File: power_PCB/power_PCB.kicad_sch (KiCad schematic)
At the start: 0 parts

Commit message: all boards routed: light rev B (SOT-23 switches, protected input), pump rev B (CSD18540 MOSFETs), power rev A1 (parts selected), brain Micro-Fit connectors + display on edge; whitelist gitignore
Light, power and pump pass DRC and ERC clean. Brain routed with 0 unconnected; remaining warnings are dangling vias, thin silk text and missing no-connect flags. All cable connectors standardized to Molex Micro-Fit 3.0. Repo now tracks only the KiCad project files, design rules, local libraries and brain 3D models.
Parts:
- added C1, C17: 100uF 35V HYBRID, Capacitor_SMD:CP_Elec_8x10.5, symbol Device:C_Polarized
- added C10, C11, C15, C2, C4, C5: 100nF 50V X7R, Capacitor_SMD:C_0805_2012Metric, symbol Device:C
- added C12, C13, C6, C7: 22uF 25V X7R, Capacitor_SMD:C_1210_3225Metric, symbol Device:C
- added C14, C8: 75pF 50V C0G 5%, Capacitor_SMD:C_0805_2012Metric, symbol Device:C
- added C16: 1uF 25V X7R, Capacitor_SMD:C_0805_2012Metric, symbol Device:C
- added C3, C9: 10uF 50V X7R, Capacitor_SMD:C_1210_3225Metric, symbol Device:C
- added D1: SMBJ15A, Diode_SMD:D_SMB, symbol Device:D_TVS
- added D2: V10P45 / 10A 45V, HydroPower:Vishay_V10P45_TO-277A_K1_A2, symbol Device:D_Schottky
- added F1: 20A FAST / PROVISIONAL, Fuse:Fuse_Littelfuse-NANO2-451_453, symbol Device:Fuse
- added F2: 5A FAST / PROVISIONAL, Fuse:Fuse_Littelfuse-NANO2-451_453, symbol Device:Fuse
- added F3, F5: 3A FAST / PROVISIONAL, Fuse:Fuse_Littelfuse-NANO2-451_453, symbol Device:Fuse
- added F4: 15A FAST / PROVISIONAL, Fuse:Fuse_Littelfuse-NANO2-451_453, symbol Device:Fuse
- added J1: 12V INPUT - 5 PAIRS, Connector_Molex:Molex_Micro-Fit_3.0_43650-1024_1x10-1MP_P3.00mm_Vertical, symbol Connector_Generic:Conn_01x10
- added J2: LIGHT BOARD, Connector_Molex:Molex_Micro-Fit_3.0_43650-0224_1x02-1MP_P3.00mm_Vertical, symbol Connector_Generic:Conn_01x02
- added J3: PUMP BOARD, Connector_Molex:Molex_Micro-Fit_3.0_43650-0324_1x03-1MP_P3.00mm_Vertical, symbol Connector_Generic:Conn_01x03
- added J4: COOLER - 3 PAIRS, Connector_Molex:Molex_Micro-Fit_3.0_43650-0624_1x06-1MP_P3.00mm_Vertical, symbol Connector_Generic:Conn_01x06
- added J5: BRAIN POWER, Connector_Molex:Molex_Micro-Fit_3.0_43650-0224_1x02-1MP_P3.00mm_Vertical, symbol Connector_Generic:Conn_01x02
- added J6: COOLER CONTROL, Connector_Molex:Molex_Micro-Fit_3.0_43650-0224_1x02-1MP_P3.00mm_Vertical, symbol Connector_Generic:Conn_01x02
- added L1: 6.8uH, Inductor_SMD:L_Coilcraft_XAL7030-682, symbol Device:L
- added L2: 10uH, Inductor_SMD:L_Coilcraft_XAL7030-103, symbol Device:L
- added Q1: CSD18540Q5B, Package_TO_SOT_SMD:TDSON-8-1, symbol Transistor_FET:CSD18540Q5B
- added R1, R5: 511k 1%, Resistor_SMD:R_0603_1608Metric, symbol Device:R
- added R10, R11: 22R, Resistor_SMD:R_0603_1608Metric, symbol Device:R
- added R12, R9: 10k, Resistor_SMD:R_0603_1608Metric, symbol Device:R
- added R2, R6: 105k 1%, Resistor_SMD:R_0603_1608Metric, symbol Device:R
- added R3, R7: 100k 0.1%, Resistor_SMD:R_0603_1608Metric, symbol Device:R
- added R4: 22.1k 0.1%, Resistor_SMD:R_0603_1608Metric, symbol Device:R
- added R8: 13.5k 0.1%, Resistor_SMD:R_0603_1608Metric, symbol Device:R
- added TP1: GND, HydroPower:TestPoint_Pad_D2.0mm_ClearSilk, symbol Connector:TestPoint
- added TP2: P12V, HydroPower:TestPoint_Pad_D2.0mm_ClearSilk, symbol Connector:TestPoint
- added TP3: +3V3, HydroPower:TestPoint_Pad_D2.0mm_ClearSilk, symbol Connector:TestPoint
- added TP4: +5V, HydroPower:TestPoint_Pad_D2.0mm_ClearSilk, symbol Connector:TestPoint
- added TP5: COOL_NEG, HydroPower:TestPoint_Pad_D2.0mm_ClearSilk, symbol Connector:TestPoint
- added U1, U2: TPS54302DDCR, Package_TO_SOT_SMD:SOT-23-6, symbol Regulator_Switching:TPS54302
- added U3: UCC27511ADBVR, Package_TO_SOT_SMD:SOT-23-6, symbol Driver_FET:UCC27511ADBV
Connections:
- new net: C14.2, R7.2, R8.1, U2.4 (FB)
- new net: C11.2, L2.1, U2.2 (SW)
- new net: R5.2, R6.1, U2.5 (EN)
- new net: C11.1, U2.6 (BOOT)
- new net: Q1.4 (G), R10.2, R11.2, R12.1
- new net: C5.1, U1.6 (BOOT)
- new net: C5.2, L1.1, U1.2 (SW)
- new net: R1.2, R2.1, U1.5 (EN)
- new net: R10.1, U3.2 (OUTH)
- new net: R11.1, U3.3 (OUTL)
- new net: C8.2, R3.2, R4.1, U1.4 (FB)
- new net +3V3: C6.1, C7.1, C8.1, J5.1 (Pin_1), L1.2, R3.1, TP3.1
- new net +5V: C12.1, C13.1, C14.1, C15.1, C16.1, J3.2 (Pin_2), L2.2, R7.1, TP4.1, U3.1 (V_{DD})
- new net COOL_12V: C17.1, D2.1 (K), F4.2, J4.1 (Pin_1), J4.2 (Pin_2), J4.3 (Pin_3)
- new net COOL_EN: J6.1 (Pin_1), R9.1, U3.6 (IN+)
- new net COOL_NEG: D2.2 (A), J4.4 (Pin_4), J4.5 (Pin_5), J4.6 (Pin_6), Q1.5 (D), TP5.1
- new net GND: C1.2, C10.2, C12.2, C13.2, C15.2, C16.2, C17.2, C2.2, C3.2, C4.2, C6.2, C7.2, C9.2, D1.2 (A2), J1.10 (Pin_10), J1.6 (Pin_6), J1.7 (Pin_7), J1.8 (Pin_8), J1.9 (Pin_9), J2.2 (Pin_2), J3.3 (Pin_3), J5.2 (Pin_2), J6.2 (Pin_2), Q1.1 (S), Q1.2 (S), Q1.3 (S), R12.2, R2.2, R4.2, R6.2, R8.2, R9.2, TP1.1, U1.1 (GND), U2.1 (GND), U3.4 (GND), U3.5 (IN-)
- new net LIGHT_12V: F2.2, J2.1 (Pin_1)
- new net LOGIC_12V: C10.1, C3.1, C4.1, C9.1, F5.2, R1.1, R5.1, U1.3 (VIN), U2.3 (VIN)
- new net P12V: C1.1, C2.1, D1.1 (A1), F1.2, F2.1, F3.1, F4.1, F5.1, TP2.1
- new net PUMP_12V: F3.2, J3.1 (Pin_1)
- new net VIN_12V: F1.1, J1.1 (Pin_1), J1.2 (Pin_2), J1.3 (Pin_3), J1.4 (Pin_4), J1.5 (Pin_5)
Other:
- note added: "1. 12V INPUT / FUSED DISTRIBUTION"
- note added: "2. 12V TO +3V3 BUCK - TPS54302"
- note added: "3. 12V TO +5V BUCK - TPS54302"
- note added: "4. COOLER SWITCH - PE8 HIGH = ON"
- note added: "5. TEST POINTS / RELEASE NOTES"
- note added: "Cooler estimate: 120W / 12V = 10A ONLY if 120W is electrical input. Confirm total current including its fan and any water circulation pump. Low-side switch: COOL_NEG must not have another ground connection. Use slow on/off control; no high-frequency PWM specified. Driver IN- grounded; IN+ and gate pulled down for disconnected control. Q1 requires heat-spreading copper; final thermal validation pe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"
- note added: "J1: pins 1-5 = +12V input; pins 6-10 = GND. Use all five 18AWG wires per polarity. J4: pins 1-3 = fused +12V; pins 4-6 = COOL_NEG. Use all three 18AWG wires per polarity. Equal wire lengths and sound crimps required; validate contact current sharing / temperature. Provisional total continuous budget: 15A at room temperature; further derating in warm enclosure. Fuses are provisional: F1 20A, F2 5A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"
- note added: "J6 pin 1 -> brain J9 pin 3 (PE8 / COOL) J6 pin 2 -> brain J9 pin 1 (GND) J5 pin 1 -> brain J10 pin 1 (3V3); pin 2 -> GND."
- note added: "PRE-LAYOUT PART SELECTION - NOT FOR FABRICATION MPN, Manufacturer and Datasheet fields assigned to every purchased PCB part. All soldered parts / connector tabs are surface mount; test points are bare copper. Current-dependent selections remain provisional until loads / temperature are measured. Brain supply is 3.3V ONLY. Verify it before connecting the brain. 5V pump rail retained pending teamma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"
- note added: "Short VIN bypass / SW loop; sense FB at output capacitors. Coilcraft XAL7030 selected. Initial rail load target 1A; validate DC bias, loop response and temperature. IC 3A is not a board rating."
- title: (none) -> HYDROPONICS - POWER DISTRIBUTION AND COOLER CONTROL

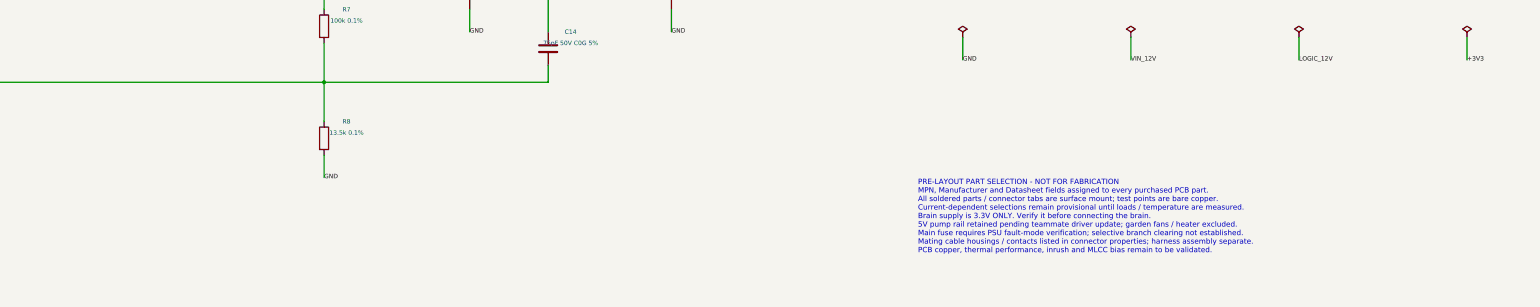
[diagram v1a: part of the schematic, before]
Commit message: Update four KiCad designs and include portable project libraries
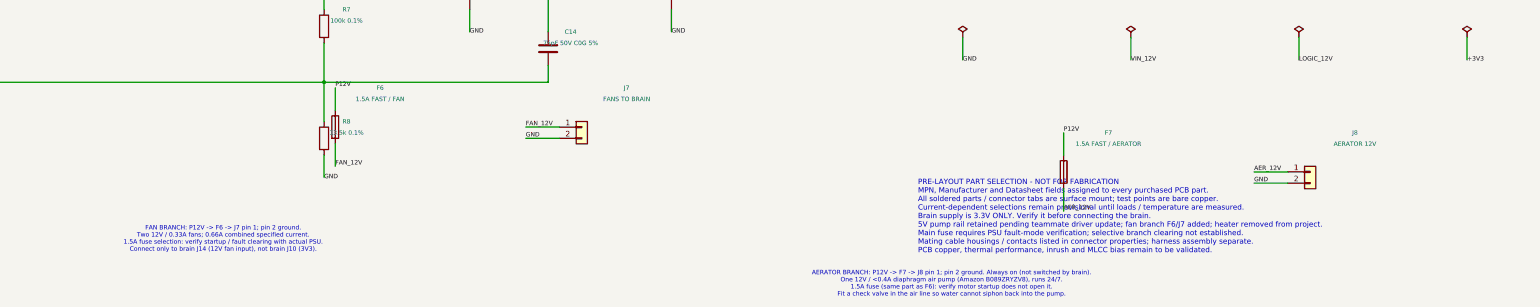
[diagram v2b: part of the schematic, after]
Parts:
- added F6: 1.5A FAST / FAN, Fuse:Fuse_1206_3216Metric, symbol Device:Fuse
- added F7: 1.5A FAST / AERATOR, Fuse:Fuse_1206_3216Metric, symbol Device:Fuse
- added J7: FANS TO BRAIN, Connector_JST:JST_XH_B2B-XH-A_1x02_P2.50mm_Vertical, symbol Connector_Generic:Conn_01x02
- added J8: AERATOR 12V, Connector_JST:JST_XH_B2B-XH-A_1x02_P2.50mm_Vertical, symbol Connector_Generic:Conn_01x02
- C1, C17: JLCPCB URL (none) -> https://jlcpcb.com/partdetail/PANASONIC-EEHZC1V101P/C454651; LCSC (none) -> C454651
- C10, C11, C15, C2, C4, C5: JLCPCB URL (none) -> https://jlcpcb.com/partdetail/MurataElectronics-GRM21BR71H1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; LCSC (none) -> C77082
- C12, C13, C6, C7: JLCPCB URL (none) -> https://jlcpcb.com/partdetail/MurataElectronics-GRM32ER71E2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; LCSC (none) -> C21397
- C14, C8: JLCPCB URL (none) -> https://jlcpcb.com/partdetail/YAGEO-CC0805JRNPO9BN750/C1138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; LCSC (none) -> C113832; MPN C0805C750J5GACTU -> CC0805JRNPO9BN750; Manufacturer KEMET -> YAGEO; Replacement Review (none) -> Yageo 75pF 50V NP0, 5%, 0805. Same nominal feedback feed-fo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; Selection Notes Selected; PCB layout and assembly sourcing pending -> Selected; layout routed; assembly sourcing pending; Sourcing Status (none) -> Catalog checked for 3 boards of each design; stock not rese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
- C16: JLCPCB URL (none) -> https://jlcpcb.com/partdetail/MurataElectronics-GRM21BR71E1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; LCSC (none) -> C77080
- C3, C9: JLCPCB URL (none) -> https://jlcpcb.com/partdetail/MurataElectronics-GRM32ER71H1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; LCSC (none) -> C77102
- D1: JLCPCB URL (none) -> https://jlcpcb.com/partdetail/Littelfuse-SMBJ15A/C83846; LCSC (none) -> C83846
- D2: JLCPCB URL (none) -> https://jlcpcb.com/partdetail/VishayIntertech-V10P45HM3_AH/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; LCSC (none) -> C6582752; MPN V10P45-M3/86A -> V10P45HM3_A/H; Manufacturer Vishay -> Vishay Intertech; Replacement Review (none) -> Vishay V10P45 automotive-grade ordering variant, 45V 10A TO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; Sourcing Status (none) -> Catalog checked for 3 boards of each design; stock not rese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
- F1: JLCPCB URL (none) -> https://jlcpcb.com/partdetail/Littelfuse-0451020MRL/C178980; LCSC (none) -> C178980
- F2: JLCPCB URL (none) -> https://jlcpcb.com/partdetail/Littelfuse-0451005MRL/C48467; LCSC (none) -> C48467
- F3: JLCPCB URL (none) -> https://jlcpcb.com/partdetail/Littelfuse-0451003MRL/C13982; LCSC (none) -> C13982; Selection Notes PROVISIONAL: 1.25A pumps nominal; verify start/stall I2t. I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 -> PROVISIONAL: 2.75A provisional combined pump running allowa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
- F4: JLCPCB URL (none) -> https://jlcpcb.com/partdetail/Littelfuse-0451015MRL/C44480; LCSC (none) -> C44480
- F5: JLCPCB URL (none) -> https://jlcpcb.com/partdetail/Littelfuse-0451003MRL/C13982; LCSC (none) -> C13982
- J1: footprint Connector_Molex:Molex_Micro-Fit_3.0_43650-1024_1x10-1MP_P3.00mm_Vertical -> Connector_Molex:Molex_Micro-Fit_3.0_43650-1015_1x10_P3.00mm_Vertical; JLCPCB URL (none) -> https://jlcpcb.com/partdetail/MOLEX-0436501015/C17337723; LCSC (none) -> C17337723; MPN 436501024 -> 0436501015; Manufacturer Molex -> MOLEX; Replacement Review (none) -> 10-circuit vertical through-hole Micro-Fit. Preserve all fi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; Selection Notes Selected SMT header; matched cable housing and contacts req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 -> Vertical Micro-Fit replacement; PCB footprint updated where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; Sourcing Status (none) -> Catalog checked for 3 boards of each design; stock not rese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
- J2: footprint Connector_Molex:Molex_Micro-Fit_3.0_43650-0224_1x02-1MP_P3.00mm_Vertical -> Connector_JST:JST_XH_B2B-XH-A_1x02_P2.50mm_Vertical; Cable Contact 430300038 (18AWG) -> SXH-001T-P0.6; MPN 436500224 -> B2B-XH-A(LF)(SN); Manufacturer Molex -> JST (XH-compatible clone OK); Mating Housing 436450200 -> XHP-2; Selection Notes Selected SMT header; matched cable housing and contacts req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 -> JST XH 2.50mm vertical THT, hand-soldered (Taiss XH kit, Am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
- J3: footprint Connector_Molex:Molex_Micro-Fit_3.0_43650-0324_1x03-1MP_P3.00mm_Vertical -> Connector_JST:JST_XH_B3B-XH-A_1x03_P2.50mm_Vertical; Cable Contact 430300007 (20-24AWG) -> SXH-001T-P0.6; MPN 436500324 -> B3B-XH-A(LF)(SN); Manufacturer Molex -> JST (XH-compatible clone OK); Mating Housing 436450300 -> XHP-3; Replacement Review (none) -> JST XH 2.50mm vertical THT, hand-soldered (Taiss XH kit, Am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; Selection Notes Selected SMT header; matched cable housing and contacts req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 -> JST XH 2.50mm vertical THT, hand-soldered (Taiss XH kit, Am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; Sourcing Status (none) -> JST XH 2.50mm vertical THT, hand-soldered (Taiss XH kit, Am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
- J4: footprint Connector_Molex:Molex_Micro-Fit_3.0_43650-0624_1x06-1MP_P3.00mm_Vertical -> Connector_Molex:Molex_Micro-Fit_3.0_43650-0615_1x06_P3.00mm_Vertical; JLCPCB URL (none) -> https://jlcpcb.com/partdetail/MOLEX-436500615/C505231; LCSC (none) -> C505231; MPN 436500624 -> 436500615; Manufacturer Molex -> MOLEX; Replacement Review (none) -> 6-circuit vertical through-hole Micro-Fit. Replace SMT foot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; Selection Notes Selected SMT header; matched cable housing and contacts req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 -> Vertical Micro-Fit replacement; PCB footprint updated where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; Sourcing Status (none) -> Catalog checked for 3 boards of each design; stock not rese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
- J5, J6: footprint Connector_Molex:Molex_Micro-Fit_3.0_43650-0224_1x02-1MP_P3.00mm_Vertical -> Connector_JST:JST_XH_B2B-XH-A_1x02_P2.50mm_Vertical; Cable Contact 430300007 (20-24AWG) -> SXH-001T-P0.6; MPN 436500224 -> B2B-XH-A(LF)(SN); Manufacturer Molex -> JST (XH-compatible clone OK); Mating Housing 436450200 -> XHP-2; Selection Notes Selected SMT header; matched cable housing and contacts req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 -> JST XH 2.50mm vertical THT, hand-soldered (Taiss XH kit, Am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
- L1: footprint Inductor_SMD:L_Coilcraft_XAL7030-682 -> HydroPower:L_Bourns_SRP7030CA_7.6x7.8mm; JLCPCB URL (none) -> https://jlcpcb.com/partdetail/BOURNS-SRP7030CA6R8M/C2047432; LCSC (none) -> C2047432; MPN XAL7030-682MEC -> SRP7030CA-6R8M; Manufacturer Coilcraft -> BOURNS; Replacement Review (none) -> Bourns SRP7030CA-6R8M: 6.8uH 20%, 42.5mohm max DCR, typical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; Selection Notes Selected shielded inductor; 20% tolerance. Verify converter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 -> 6.8uH 20%; Bourns SRP7030CA; max DCR 42.5mohm. Check therma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; Sourcing Status (none) -> Catalog checked for 3 boards of each design; stock not rese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
- L2: JLCPCB URL (none) -> https://jlcpcb.com/partdetail/Coilcraft-XAL7030103MEC/C1919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; LCSC (none) -> C19191652
- Q1: JLCPCB URL (none) -> https://jlcpcb.com/partdetail/TexasInstruments-CSD18540Q5B/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; LCSC (none) -> C86513
- R1, R5: JLCPCB URL (none) -> https://jlcpcb.com/partdetail/YAGEO-RC0603FR07511KL/C188257; LCSC (none) -> C188257; Selection Notes Selected; PCB layout and assembly sourcing pending -> Selected; layout routed; assembly sourcing pending
- R10, R11: JLCPCB URL (none) -> https://jlcpcb.com/partdetail/YAGEO-RC0603FR0722RL/C107701; LCSC (none) -> C107701; Selection Notes Selected; PCB layout and assembly sourcing pending -> Selected; layout routed; assembly sourcing pending
- R12, R9: JLCPCB URL (none) -> https://jlcpcb.com/partdetail/YAGEO-RC0603FR0710KL/C98220; LCSC (none) -> C98220; Selection Notes Selected; PCB layout and assembly sourcing pending -> Selected; layout routed; assembly sourcing pending
- R2, R6: JLCPCB URL (none) -> https://jlcpcb.com/partdetail/YAGEO-RT0603BRD07105KL/C861072; LCSC (none) -> C861072; MPN RC0603FR-07105KL -> RT0603BRD07105KL; Rating (none) -> 105kohm 0.1%, 0603, 100mW; Replacement Review (none) -> Yageo 105kohm 0.1% 0603 thin-film replaces 105kohm 1% thick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; Selection Notes Selected; PCB layout and assembly sourcing pending -> Selected; layout routed; assembly sourcing pending; Sourcing Status (none) -> Catalog checked for 3 boards of each design; stock not rese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
- R3, R7: JLCPCB URL (none) -> https://jlcpcb.com/partdetail/YAGEO-RT0603BRD07100KL/C122538; LCSC (none) -> C122538; Selection Notes Selected; PCB layout and assembly sourcing pending -> Selected; layout routed; assembly sourcing pending
- R4: JLCPCB URL (none) -> https://jlcpcb.com/partdetail/YAGEO-RT0603BRD0722K1L/C723484; LCSC (none) -> C723484; Selection Notes Selected; PCB layout and assembly sourcing pending -> Selected; layout routed; assembly sourcing pending
- R8: JLCPCB URL (none) -> https://jlcpcb.com/partdetail/YAGEO-RT0603BRD0713K5L/C861118; LCSC (none) -> C861118; Selection Notes Selected; PCB layout and assembly sourcing pending -> Selected; layout routed; assembly sourcing pending
- U1, U2: JLCPCB URL (none) -> https://jlcpcb.com/partdetail/TexasInstruments-TPS54302DDCR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; LCSC (none) -> C311983; Selection Notes Selected; PCB layout and assembly sourcing pending -> Selected; layout routed; assembly sourcing pending
- U3: JLCPCB URL (none) -> https://jlcpcb.com/partdetail/TexasInstruments-UCC27511ADBV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; LCSC (none) -> C2676982; Selection Notes Selected; PCB layout and assembly sourcing pending -> Selected; layout routed; assembly sourcing pending
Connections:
- net GND: now also J7.2 (Pin_2), J8.2 (Pin_2)
- net P12V: now also F6.1, F7.1
- new net AER_12V: F7.2, J8.1 (Pin_1)
- new net FAN_12V: F6.2, J7.1 (Pin_1)
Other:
- note added: "AERATOR BRANCH: P12V -> F7 -> J8 pin 1; pin 2 ground. Always on (not switched by brain). One 12V / <0.4A diaphragm air pump (Amazon B089ZRYZV8), runs 24/7. 1.5A fuse (same part as F6): verify motor startup does not open it. Fit a check valve in the air line so water cannot siphon back into the pump."
- note added: "FAN BRANCH: P12V -> F6 -> J7 pin 1; pin 2 ground. Two 12V / 0.33A fans; 0.66A combined specified current. 1.5A fuse selection: verify startup / fault clearing with actual PSU. Connect only to brain J14 (12V fan input), not brain J10 (3V3)."
